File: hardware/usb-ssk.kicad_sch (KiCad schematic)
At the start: 0 parts

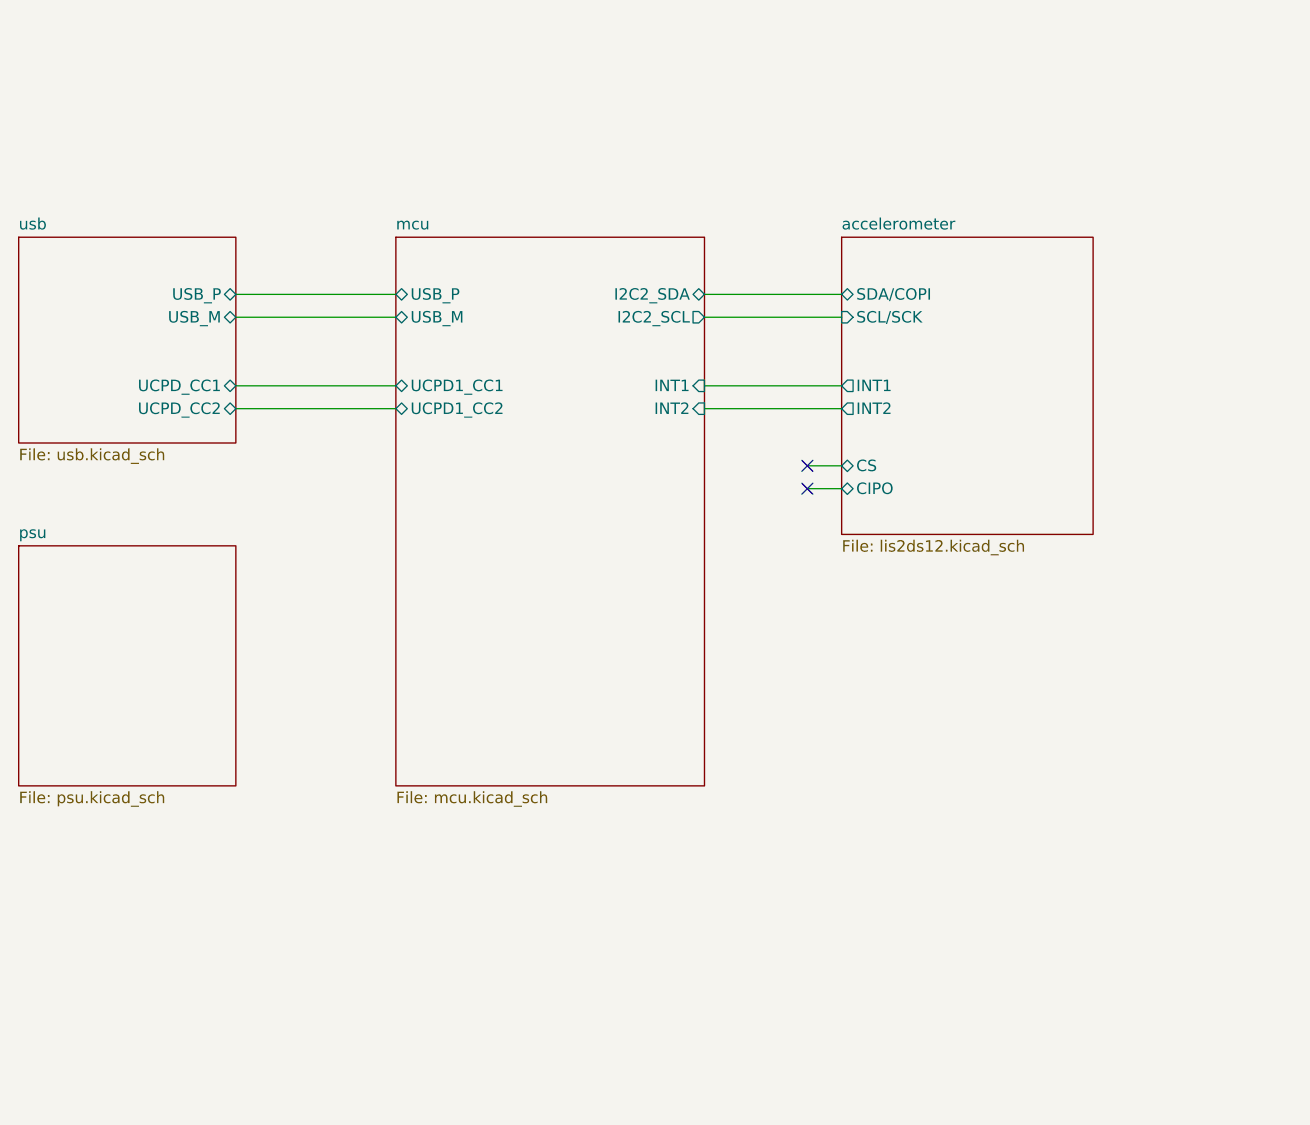
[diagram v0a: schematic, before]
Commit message: new hardware layout for IIS2ICLX
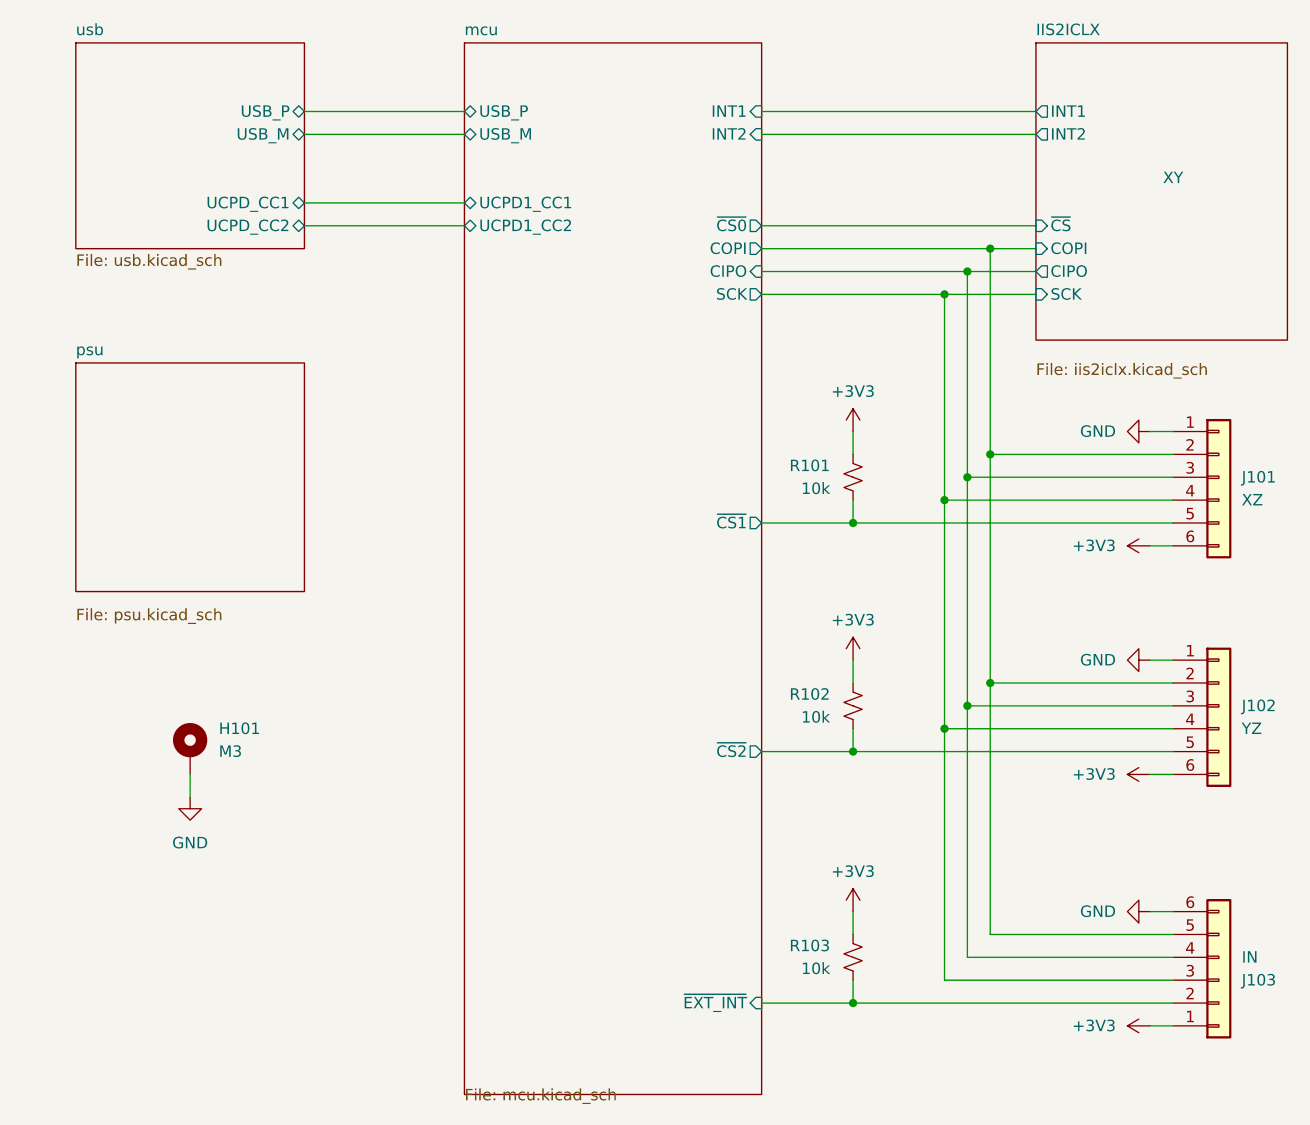
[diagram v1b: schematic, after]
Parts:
- added H101: M3, MountingHole:MountingHole_3.2mm_M3_DIN965_Pad, symbol Mechanical:MountingHole_Pad
- added J101: XZ, easyeda2kicad:FPC-SMD_6P-P0.50_XUNPU_FPC-05F-6PH20, symbol Connector_Generic:Conn_01x06
- added J102: YZ, easyeda2kicad:FPC-SMD_6P-P0.50_XUNPU_FPC-05F-6PH20, symbol Connector_Generic:Conn_01x06
- added J103: IN, easyeda2kicad:FPC-SMD_6P-P0.50_XUNPU_FPC-05F-6PH20, symbol Connector_Generic:Conn_01x06
- added R101, R102, R103: 10k, Resistor_SMD:R_0402_1005Metric, symbol Device:R_Small_US
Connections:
- new net +3V3: J101.6 (Pin_6), J102.6 (Pin_6), J103.1 (Pin_1), R101.1, R102.1, R103.1
- new net GND: H101.1, J101.1 (Pin_1), J102.1 (Pin_1), J103.6 (Pin_6)
- new net IIS2ICLX/CIPO: J101.3 (Pin_3), J102.3 (Pin_3), J103.4 (Pin_4)
- new net IIS2ICLX/COPI: J101.2 (Pin_2), J102.2 (Pin_2), J103.5 (Pin_5)
- new net IIS2ICLX/SCK: J101.4 (Pin_4), J102.4 (Pin_4), J103.3 (Pin_3)
- new net mcu/~{CS1}: J101.5 (Pin_5), R101.2
- new net mcu/~{CS2}: J102.5 (Pin_5), R102.2
- new net mcu/~{EXT_INT}: J103.2 (Pin_2), R103.2
- no-connect marks 2 -> 0
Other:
- removed sheet accelerometer
- added sheet IIS2ICLX (iis2iclx.kicad_sch)
- sheet mcu ports: added CIPO, COPI, SCK, ~{CS0}, ~{CS1}, ~{CS2}, ~{EXT_INT}; removed I2C2_SCL, I2C2_SDA
- note added: "XY"
